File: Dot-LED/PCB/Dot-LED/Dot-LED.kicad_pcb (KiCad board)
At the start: 4 copper layers, 10 x 10 mm, 1 part

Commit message: Update DotLED Schem
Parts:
- removed N1: V20220506, SquantorLabels:Label_Generic
- added C1: 24nF, SamacSys_Parts:CAPC1005X55N, F.Cu at (140.1, 51.5)
- added C10: 24nF, SamacSys_Parts:CAPC1005X55N, F.Cu at (131.1, 56.1)
- added C11: 24nF, SamacSys_Parts:CAPC1005X55N, F.Cu at (131.4, 50.7)
- added C12: 1uF, Capacitor_SMD:C_0603_1608Metric_Pad1.08x0.95mm_HandSolder, F.Cu at (120.9, 53.8)
- added C13: 100nf, Capacitor_SMD:C_0603_1608Metric_Pad1.08x0.95mm_HandSolder, F.Cu at (120.9, 55.7)
- added C14: 10uf, Capacitor_SMD:C_0603_1608Metric_Pad1.08x0.95mm_HandSolder, B.Cu at (114.3, 50.1)
- added C15: 10uf, Capacitor_SMD:C_0603_1608Metric_Pad1.08x0.95mm_HandSolder, B.Cu at (136.0, 45.1)
- added C16: 10uf, Capacitor_SMD:C_0603_1608Metric_Pad1.08x0.95mm_HandSolder, B.Cu at (133.0, 67.2)
- added C17: 1uF, Capacitor_SMD:C_0603_1608Metric_Pad1.08x0.95mm_HandSolder, F.Cu at (131.2, 61.0)
- added C18: 100nf, Capacitor_SMD:C_0603_1608Metric_Pad1.08x0.95mm_HandSolder, B.Cu at (120.8, 66.9)
- added C19: 1uF, Capacitor_SMD:C_0603_1608Metric_Pad1.08x0.95mm_HandSolder, B.Cu at (118.8, 45.4)
- added C2: 24nF, SamacSys_Parts:CAPC1005X55N, F.Cu at (134.5, 50.5)
- added C20: 100nf, Capacitor_SMD:C_0603_1608Metric_Pad1.08x0.95mm_HandSolder, B.Cu at (118.8, 47.2)
- added C3: 1uF, Capacitor_SMD:C_0603_1608Metric_Pad1.08x0.95mm_HandSolder, F.Cu at (124.7, 55.7)
- added C4: 100nf, Capacitor_SMD:C_0603_1608Metric_Pad1.08x0.95mm_HandSolder, F.Cu at (124.7, 53.8)
- added C5: 100nf, Capacitor_SMD:C_0603_1608Metric_Pad1.08x0.95mm_HandSolder, B.Cu at (139.9, 55.1)
- added C6: 1uF, Capacitor_SMD:C_0603_1608Metric_Pad1.08x0.95mm_HandSolder, B.Cu at (137.8, 46.6)
- added C7: 100nf, Capacitor_SMD:C_0603_1608Metric_Pad1.08x0.95mm_HandSolder, B.Cu at (134.2, 44.3)
- added C8: 100nf, Capacitor_SMD:C_0603_1608Metric_Pad1.08x0.95mm_HandSolder, F.Cu at (116.8, 63.5)
- added C9: 100nf, Capacitor_SMD:C_0603_1608Metric_Pad1.08x0.95mm_HandSolder, F.Cu at (137.3, 63.9)
- added CON1: SJ1-3523N, digikey-footprints:Headphone_Jack_3.5mm_SJ1-3523N, F.Cu at (127.0, 47.0)
- added D1: PMEG2020EPK,315, SamacSys_Parts:PMEG2020EPK315, F.Cu at (128.5, 61.5)
- added D2: PMEG2020EPK,315, SamacSys_Parts:PMEG2020EPK315, F.Cu at (125.5, 61.5)
- added D3: LED, LED_SMD:LED_0603_1608Metric_Pad1.05x0.95mm_HandSolder, B.Cu at (112.6, 55.5)
- added Data1: RCW-0C, digikey-footprints:PROBE_PAD_1206, F.Cu at (115.6, 55.1)
- added GND1: RCW-0C, digikey-footprints:PROBE_PAD_1206, F.Cu at (115.6, 52.4)
- added IC1: ESP32-C3, SamacSys_Parts:QFN50P500X500X90-33N-D, F.Cu at (137.7, 56.8)
- added IC2: MCP73831T-2ACI_OT, SamacSys_Parts:SOT95P270X145-5N, B.Cu at (114.5, 61.0)
- added IO1: 1508-0-57-15-00-00-03-0, digikey-footprints:Test-Point-Pin_Drill2.79mm, F.Cu at (55.4, 25.2)
- added IO2: 1508-0-57-15-00-00-03-0, digikey-footprints:Test-Point-Pin_Drill2.79mm, F.Cu at (55.4, 32.3)
- added IO3: 1508-0-57-15-00-00-03-0, digikey-footprints:Test-Point-Pin_Drill2.79mm, F.Cu at (62.5, 25.2)
- added IO4: 1508-0-57-15-00-00-03-0, digikey-footprints:Test-Point-Pin_Drill2.79mm, F.Cu at (62.5, 32.3)
- added IO6: 1508-0-57-15-00-00-03-0, digikey-footprints:Test-Point-Pin_Drill2.79mm, F.Cu at (69.6, 25.2)
- added IO7: 1508-0-57-15-00-00-03-0, digikey-footprints:Test-Point-Pin_Drill2.79mm, F.Cu at (69.6, 32.3)
- added IO8: 1508-0-57-15-00-00-03-0, digikey-footprints:Test-Point-Pin_Drill2.79mm, F.Cu at (76.7, 25.2)
- added IO9: 1508-0-57-15-00-00-03-0, digikey-footprints:Test-Point-Pin_Drill2.79mm, F.Cu at (76.7, 32.3)
- added L1: 2nH, SamacSys_Parts:LQG15WH0N7B02D, B.Cu at (140.2, 57.7)
- added L2: DFE252012PD-1R0M=P2, SamacSys_Parts:DFE2HCAH1R0MJ0L, F.Cu at (123.8, 58.5)
- added P1: USB_C_Plug, digikey-footprints:USB-C_Female_E8124-015-01, F.Cu at (127.0, 65.8)
- added R1: 0, SamacSys_Parts:RESC1608X55N, F.Cu at (138.1, 52.2)
- added R10: 1.5k, SamacSys_Parts:RESC1608X55N, B.Cu at (113.3, 52.9)
- added R11: 4.3k, SamacSys_Parts:RESC1608X55N, B.Cu at (115.5, 64.5)
- added R2: 15k, SamacSys_Parts:RESC1608X55N, F.Cu at (138.1, 61.3)
- added R3: 15k, SamacSys_Parts:RESC1608X55N, F.Cu at (133.4, 59.0)
- added R4: 0, SamacSys_Parts:RESC1608X55N, F.Cu at (133.6, 55.5)
- added R5: 1, SamacSys_Parts:RESC1608X55N, F.Cu at (126.9, 51.3)
- added R6: 511k, SamacSys_Parts:RESC1608X55N, F.Cu at (128.5, 56.5)
- added R7: 91k, SamacSys_Parts:RESC1608X55N, F.Cu at (130.0, 58.0)
- added R8: 15k, SamacSys_Parts:RESC1608X55N, B.Cu at (135.4, 67.0)
- added R9: 15k, SamacSys_Parts:RESC1608X55N, B.Cu at (118.4, 66.3)
- added S1: PTS815_SJM_250_SMTR_LFS, SamacSys_Parts:PTS815SJM250SMTRLFS, F.Cu at (119.5, 63.5)
- added S2: PTS815_SJM_250_SMTR_LFS, SamacSys_Parts:PTS815SJM250SMTRLFS, F.Cu at (134.5, 64.0)
- added U1: 3034, SamacSys_Parts:3034, B.Cu at (127.1, 55.6)
- added U3: TPS631000DRLR, SamacSys_Parts:SOTFL50P160X60-8N, F.Cu at (126.8, 58.5)
- added VCC1: RCW-0C, digikey-footprints:PROBE_PAD_1206, F.Cu at (115.7, 57.9)
- added Y1: 32.768Khz, SamacSys_Parts:RH1002500012F1010TR, F.Cu at (131.2, 53.4)
- added Y2: RH100-40.000-12-F-1010-TR, SamacSys_Parts:RH1002500012F1010TR, F.Cu at (137.2, 49.6)
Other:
- board size 10 x 10 mm -> 32 x 32 mm

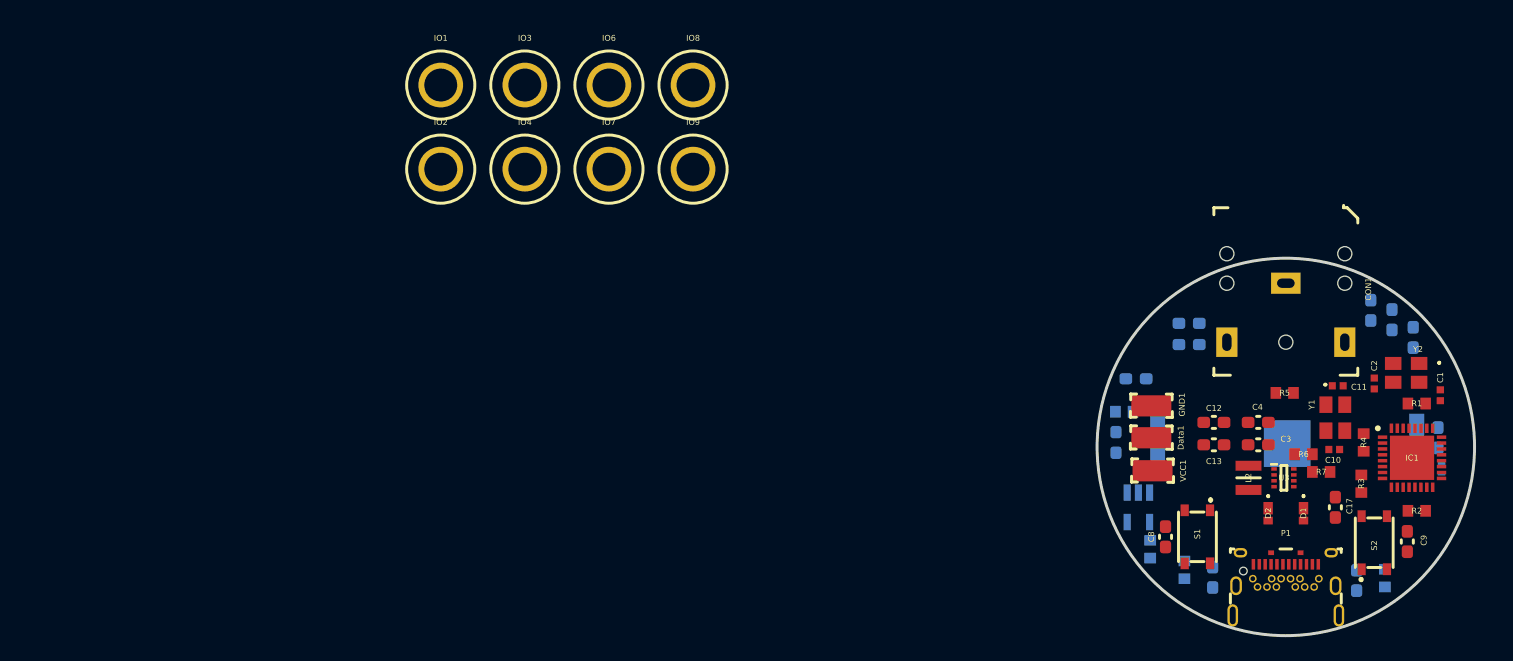
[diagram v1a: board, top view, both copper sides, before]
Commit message: update DotLED
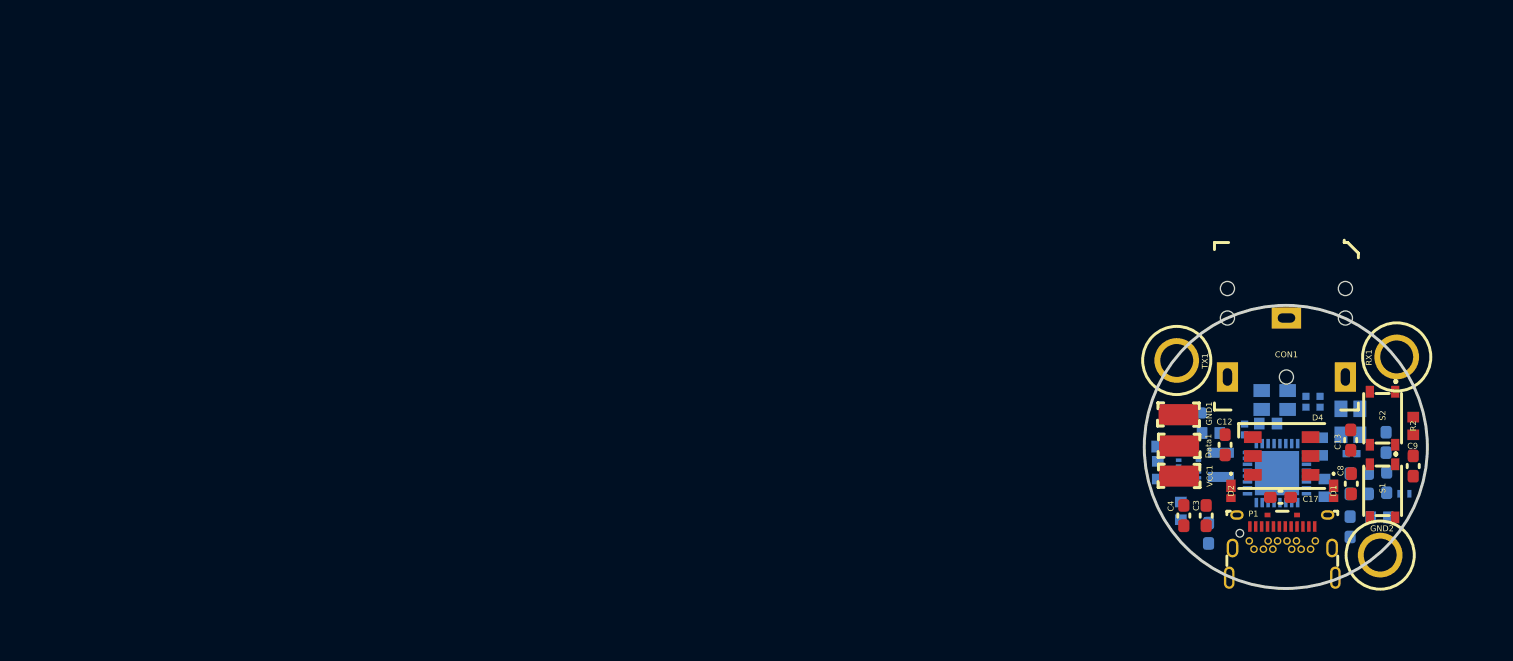
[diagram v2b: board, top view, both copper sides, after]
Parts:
- removed C19: 1uF, Capacitor_SMD:C_0603_1608Metric_Pad1.08x0.95mm_HandSolder
- removed C20: 100nf, Capacitor_SMD:C_0603_1608Metric_Pad1.08x0.95mm_HandSolder
- removed D3: LED, LED_SMD:LED_0603_1608Metric_Pad1.05x0.95mm_HandSolder
- removed IC2: MCP73831T-2ACI_OT, SamacSys_Parts:SOT95P270X145-5N
- removed IO2, IO3, IO4, IO8, IO9: 1508-0-57-15-00-00-03-0, digikey-footprints:Test-Point-Pin_Drill2.79mm
- removed R10: 1.5k, SamacSys_Parts:RESC1608X55N
- removed R11: 4.3k, SamacSys_Parts:RESC1608X55N
- removed U1: 3034, SamacSys_Parts:3034
- added D4: WS2813, LED_SMD:LED_WS2812_PLCC6_5.0x5.0mm_P1.6mm, F.Cu at (126.7, 56.6)
- C1, C10, C11, C2, IC1, L2, R1, R3, R4, R5, R6, R7, U3, Y1, Y2: moved to B.Cu
- moved GND2 89.1 mm to (135.0, 65.0)
- moved RX1 68.7 mm to (136.4, 48.2)
- moved TX1 53.5 mm to (117.8, 48.5)
- moved C1 16.9 mm to (123.5, 54.4)
- moved C8 16.4 mm to (132.6, 59.0), turned to -90 degrees
- moved S1 16.2 mm to (135.2, 59.6)
- moved C15 14.3 mm to (132.4, 59.0)
- moved R7 13.9 mm to (116.2, 57.9), turned to -90 degrees
- moved C6 13.0 mm to (134.0, 59.0)
- moved R1 12.7 mm to (125.5, 53.9), turned to 180 degrees
- moved R6 11.7 mm to (116.8, 55.9), turned to 180 degrees
- moved C13 11.6 mm to (132.5, 55.3), turned to 90 degrees
- moved IC1 11.5 mm to (126.2, 58.1), turned to 180 degrees
- moved Y2 11.4 mm to (126.0, 51.9), turned to 0 degrees
- moved C7 11.3 mm to (135.5, 55.5)
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- renumbered IO1 to GND2, IO7 to RX1, IO6 to TX1
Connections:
- net /Battery_Regulator/VDD_IN renamed 5V
- D1 pad 2: /Battery_Regulator/VBAT -> /Buck_Boost/V_Bat
- GND2 pad 1: D1 -> GND
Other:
- board size 32 x 32 mm -> 24 x 24 mm

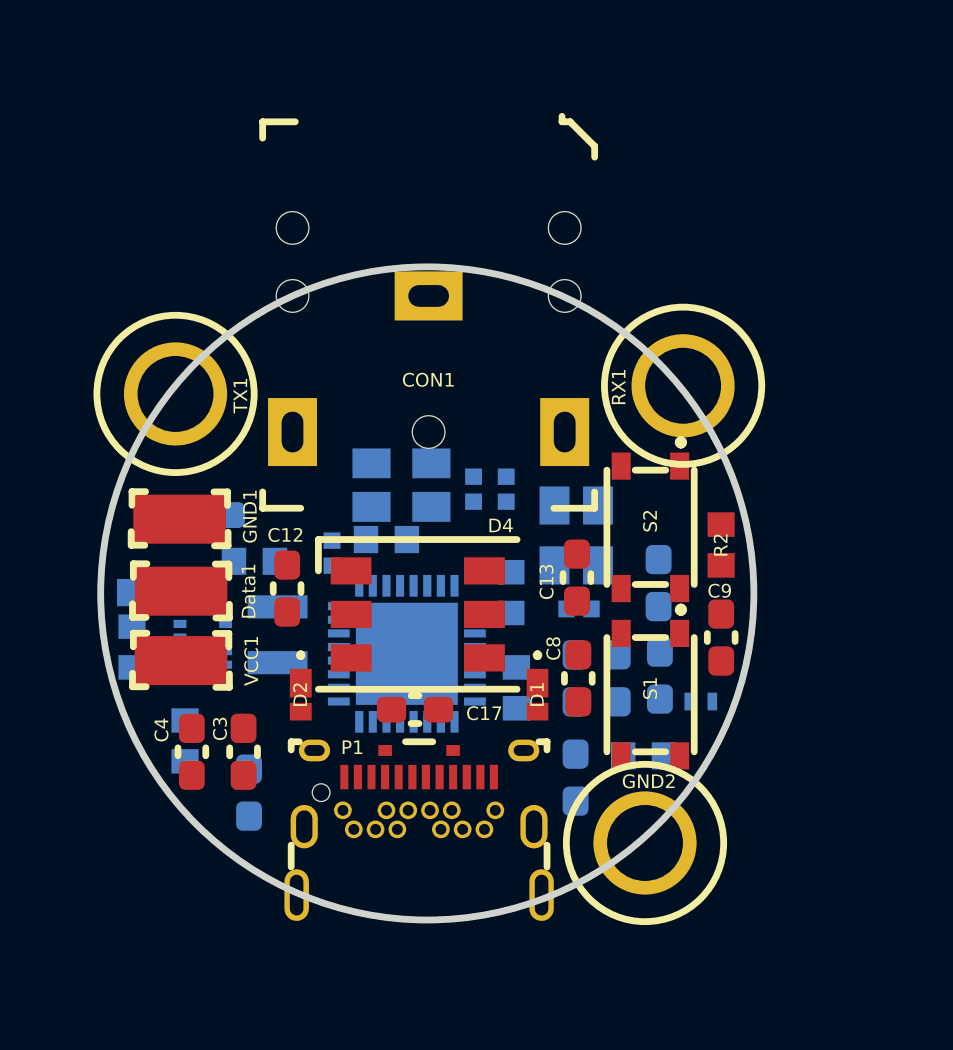
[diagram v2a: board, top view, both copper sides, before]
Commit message: Init layout for DotLED
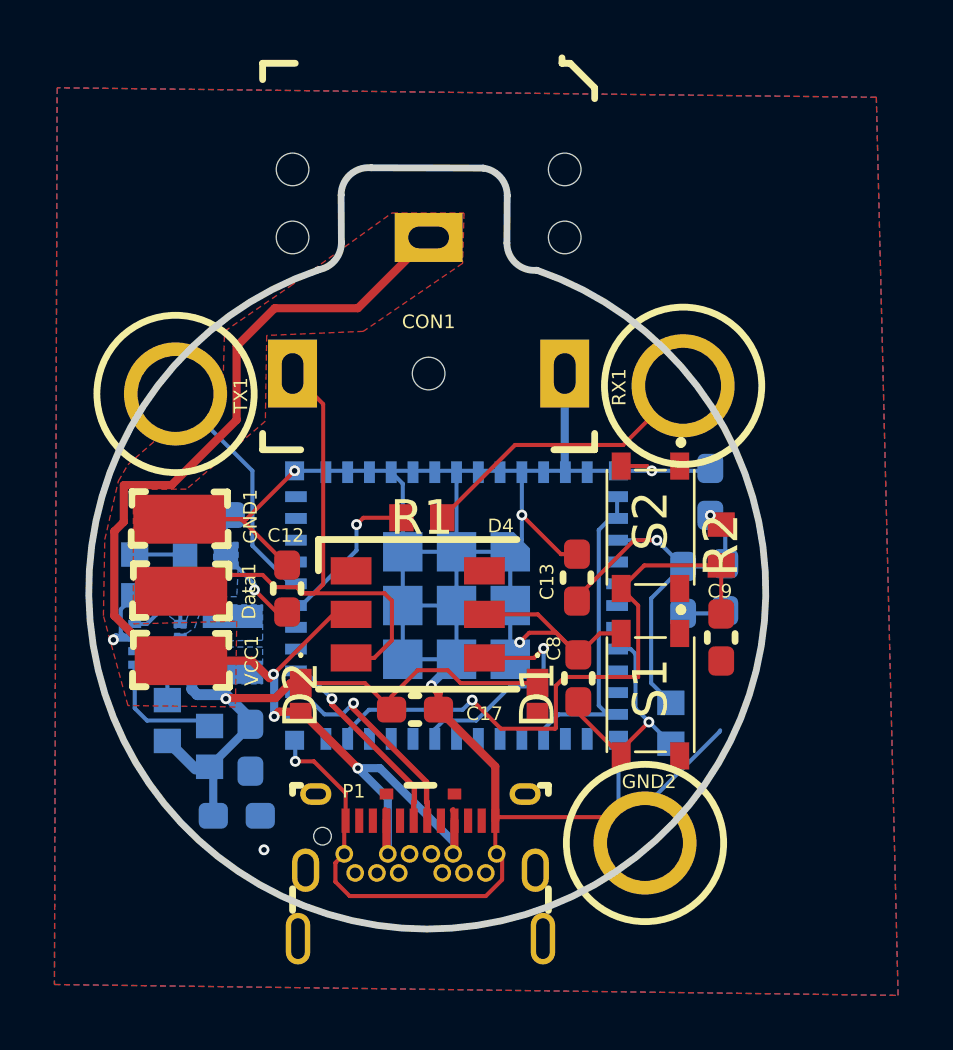
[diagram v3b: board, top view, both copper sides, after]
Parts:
- removed C1, C10, C11, C2: 24nF, SamacSys_Parts:CAPC1005X55N
- removed C3: 1uF, Capacitor_SMD:C_0603_1608Metric_Pad1.08x0.95mm_HandSolder
- removed C4, C5: 100nf, Capacitor_SMD:C_0603_1608Metric_Pad1.08x0.95mm_HandSolder
- removed IC1: ESP32-C3, SamacSys_Parts:QFN50P500X500X90-33N-D
- removed L1: 2nH, SamacSys_Parts:LQG15WH0N7B02D
- removed R4: 0, SamacSys_Parts:RESC1608X55N
- removed R5: 1, SamacSys_Parts:RESC1608X55N
- removed Y1: 32.768Khz, SamacSys_Parts:RH1002500012F1010TR
- removed Y2: RH100-40.000-12-F-1010-TR, SamacSys_Parts:RH1002500012F1010TR
- added U1: ESP32-C3-MINI-1, Espressif:ESP32-C3-MINI-1U, B.Cu at (128.1, 55.6)
- R1: value 0 -> 1; moved to F.Cu
- moved R8 17.5 mm to (117.5, 60.5), turned to -90 degrees
- moved C16 12.5 mm to (120.0, 64.0), turned to 180 degrees
- moved R3 5.82 mm to (135.9, 60.6), turned to 90 degrees
- moved C6 5.18 mm to (137.9, 55.6)
- moved C15 5.12 mm to (136.4, 55.8)
- moved C7 3.85 mm to (137.4, 52.1), turned to -90 degrees
- moved R7 2.65 mm to (116.2, 55.2)
- moved R6 2.45 mm to (118.8, 54.5)
- moved CON1 2.15 mm to (127.0, 47.8)
- moved L2 1.69 mm to (119.8, 57.8)
- moved U3 1.66 mm to (117.1, 57.8)
- moved C18 1.65 mm to (120.5, 61.5)
- moved P1 1.60 mm to (126.8, 64.2)
- moved R1 1.53 mm to (126.8, 53.1)
- moved R9 0.92 mm to (119.0, 61.5)
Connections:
- CON1 pad 1: 3V3_VCC -> 5V
- CON1 pad 2: D5 -> D5_out
- D4 pad 3: D5 -> D5_out
- Data1 pad 1: D5 -> D5_out
- R1 pad 1: Net-(IC1-XTAL_N) -> RX_D7
- VCC1 pad 1: 3V3_VCC -> 5V
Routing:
- net GND: track 0.00 -> 116.7 mm, vias 0 -> 8
- net 5V: track 0.00 -> 49.1 mm, vias 0 -> 3
- net 3V3_VCC: track 0.00 -> 40.3 mm, vias 0 -> 3
- net D9: track 0.00 -> 22.9 mm, vias 0 -> 1
- net VIN: track 0.00 -> 22.3 mm, vias 0 -> 1
- net D5_out: track 0.00 -> 20.7 mm
- net Net-(U1-GND-Pad1): track 0.00 -> 12.2 mm
- net RX_D7: track 0.00 -> 10.7 mm
- net TX_D6: track 0.00 -> 8.93 mm
- net EN: track 0.00 -> 8.89 mm, vias 0 -> 1
- net D5: track 0.00 -> 8.59 mm, vias 0 -> 1
- net /ESP32C3_MCU/ESP_DN: track 0.00 -> 7.95 mm, vias 0 -> 1
- net /ESP32C3_MCU/ESP_DP: track 0.00 -> 7.49 mm, vias 0 -> 1
- net Net-(U1-GPIO20/U0RXD): track 0.00 -> 5.77 mm, vias 0 -> 1
- net Net-(U3-FB): track 0.00 -> 5.33 mm
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- added copper zone on B.Cu, net 3V3_VCC
- added copper zone on F.Cu, net 5V
- added copper zone on B.Cu, net GND
- added copper zone on F.Cu, net GND
- added copper zone on B.Cu, net Net-(U3-LX1)
- added copper zone on B.Cu, net Net-(U3-LX2)
- added copper zone on B.Cu, net VIN
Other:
- board size 24 x 24 mm -> 24.9 x 28 mm

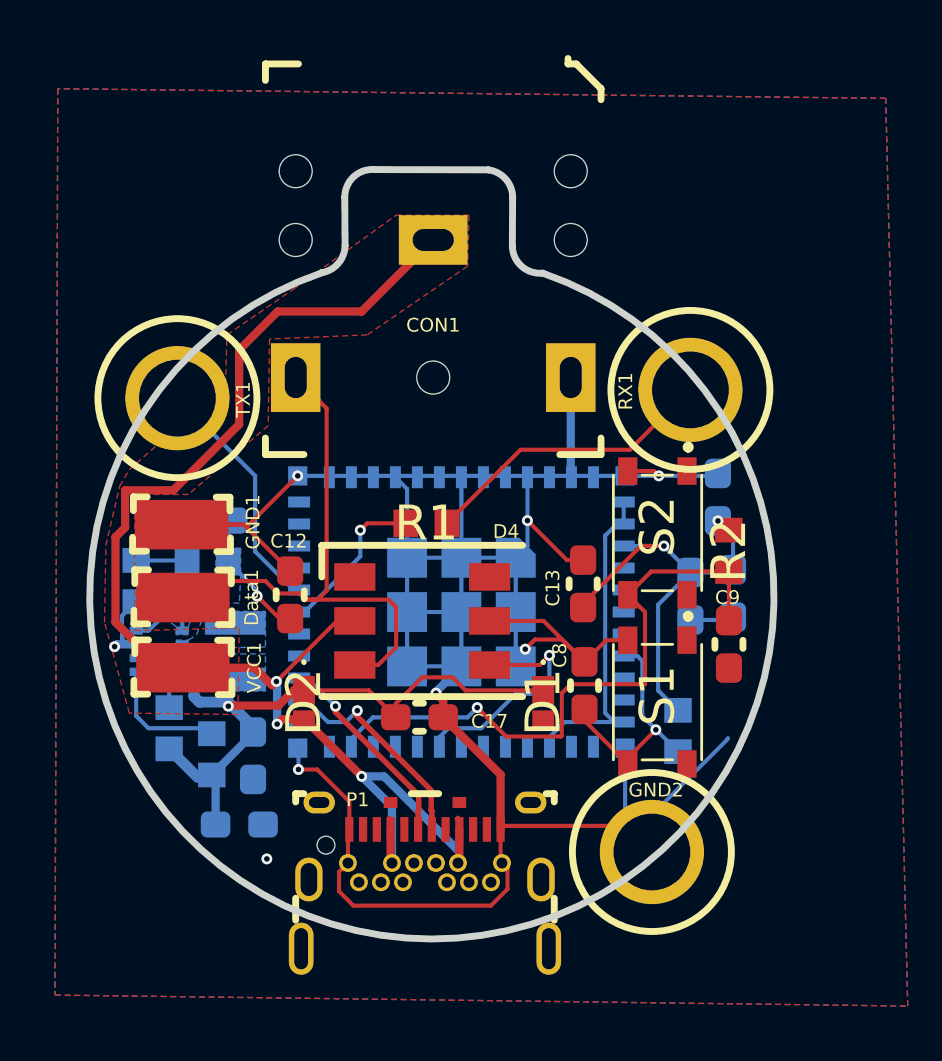
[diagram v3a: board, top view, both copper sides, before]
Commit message: Update Vreg to in-stock component
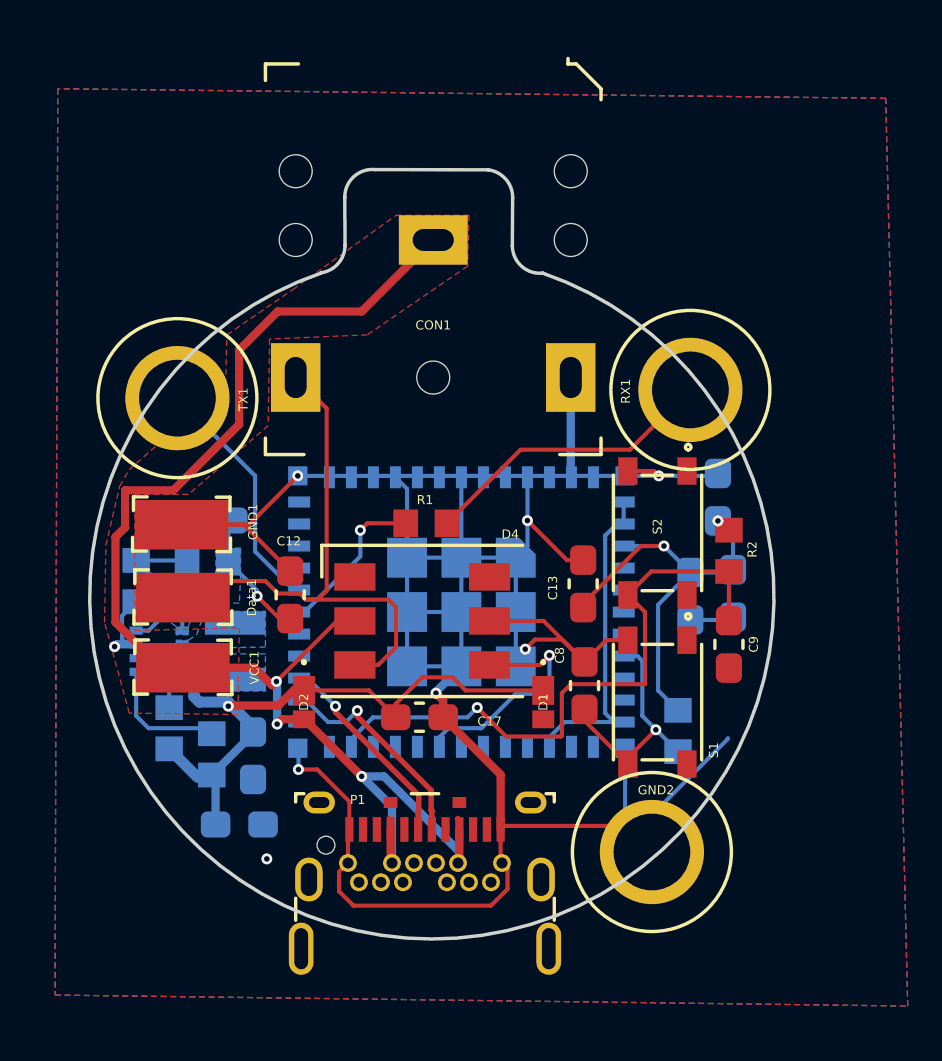
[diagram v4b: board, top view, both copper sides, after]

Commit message: more small changes
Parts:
- removed L2: DFE252012PD-1R0M=P2, SamacSys_Parts:DFE2HCAH1R0MJ0L
- removed R8, R9: 15k, SamacSys_Parts:RESC1608X55N
- removed U3: TPS631000DRLR, SamacSys_Parts:SOTFL50P160X60-8N
- added IC1: TPS631010YBGR, SamacSys_Parts:BGA8C40P2X4_86X176X50, B.Cu at (117.6, 57.9)
- added L1: DFE252012PD-1R0M=P2, SamacSys_Parts:DFE2HCAH1R0MJ0L, F.Cu at (119.9, 57.6)
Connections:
- net 3V3_VCC renamed SW
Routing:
- net Net-(U3-EN): track 4.62 -> 0.00 mm
- net Net-(IC1-FB): track 5.33 -> 1.87 mm
- net SW: track 40.3 -> 37.1 mm
- net GND: track 116.7 -> 113.7 mm, vias 8 -> 7
- net Net-(U3-MODE): track 2.54 -> 0.00 mm
- added copper zone on B.Cu, net (none)
- removed copper zone on B.Cu, net Net-(U3-LX1)
- removed copper zone on B.Cu, net Net-(U3-LX2)
